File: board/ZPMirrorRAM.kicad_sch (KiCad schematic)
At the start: 17 parts, among them IC1 74LS189, IC2 74LS189, IC3 74LS189, IC4 74LS189, U13 74F08, U24 74F20, U25 74F02, U26 74LS154, U27 74F138

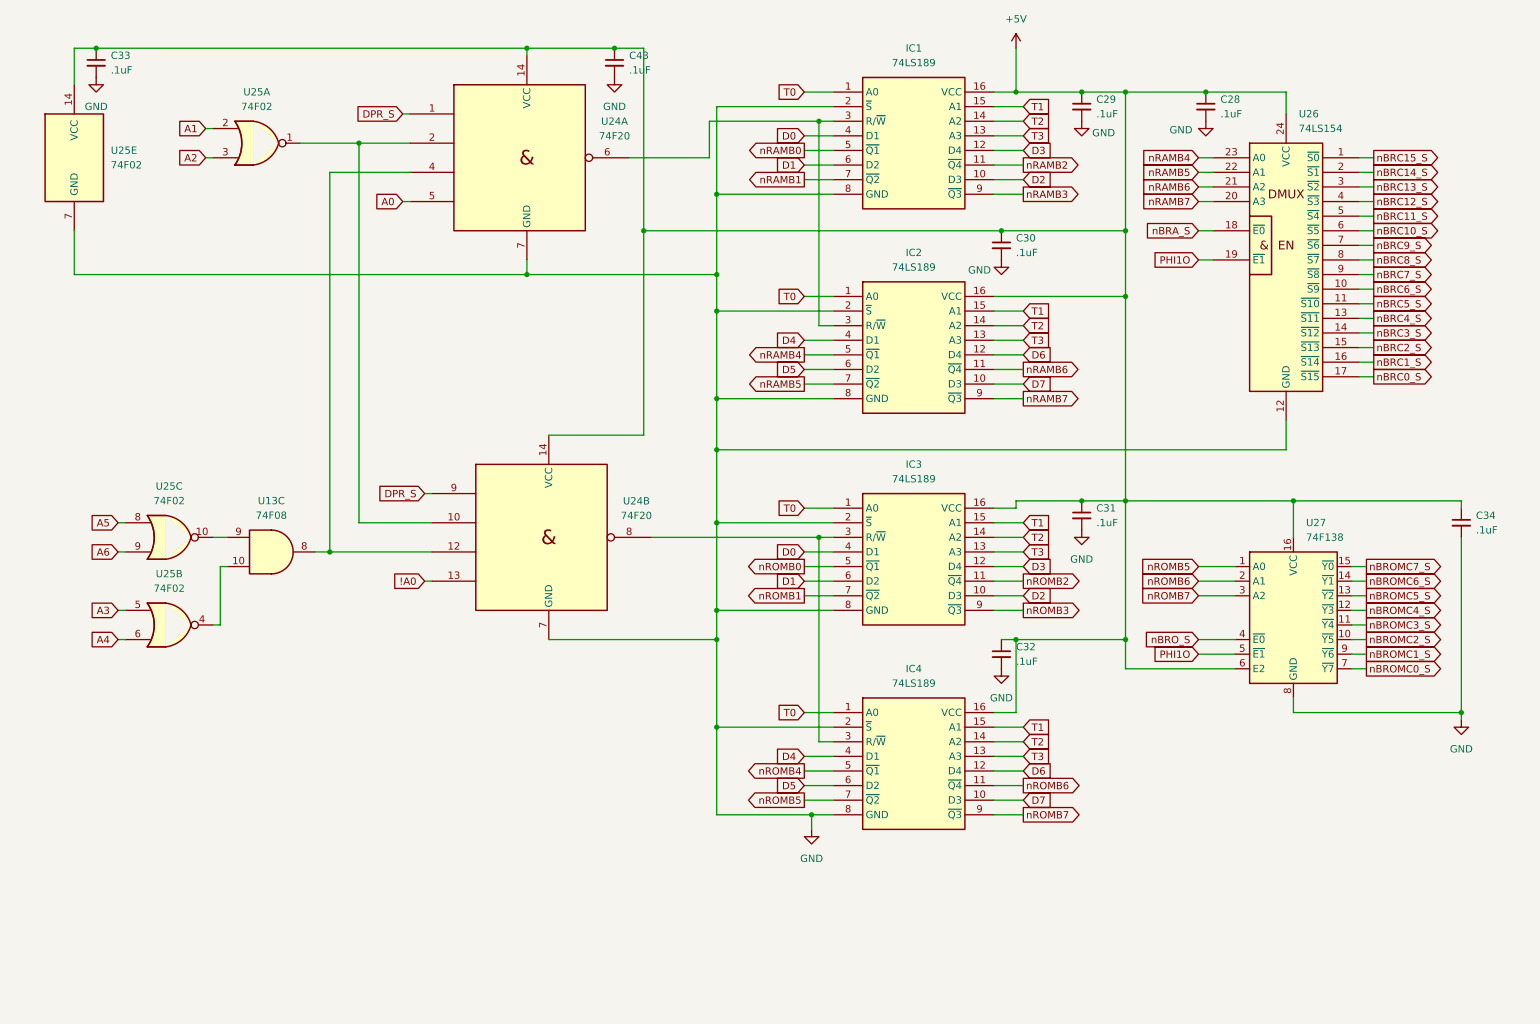
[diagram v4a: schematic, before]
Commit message: Schematic Bus updates, silkscreen updates, position tweaks, and other corrections.
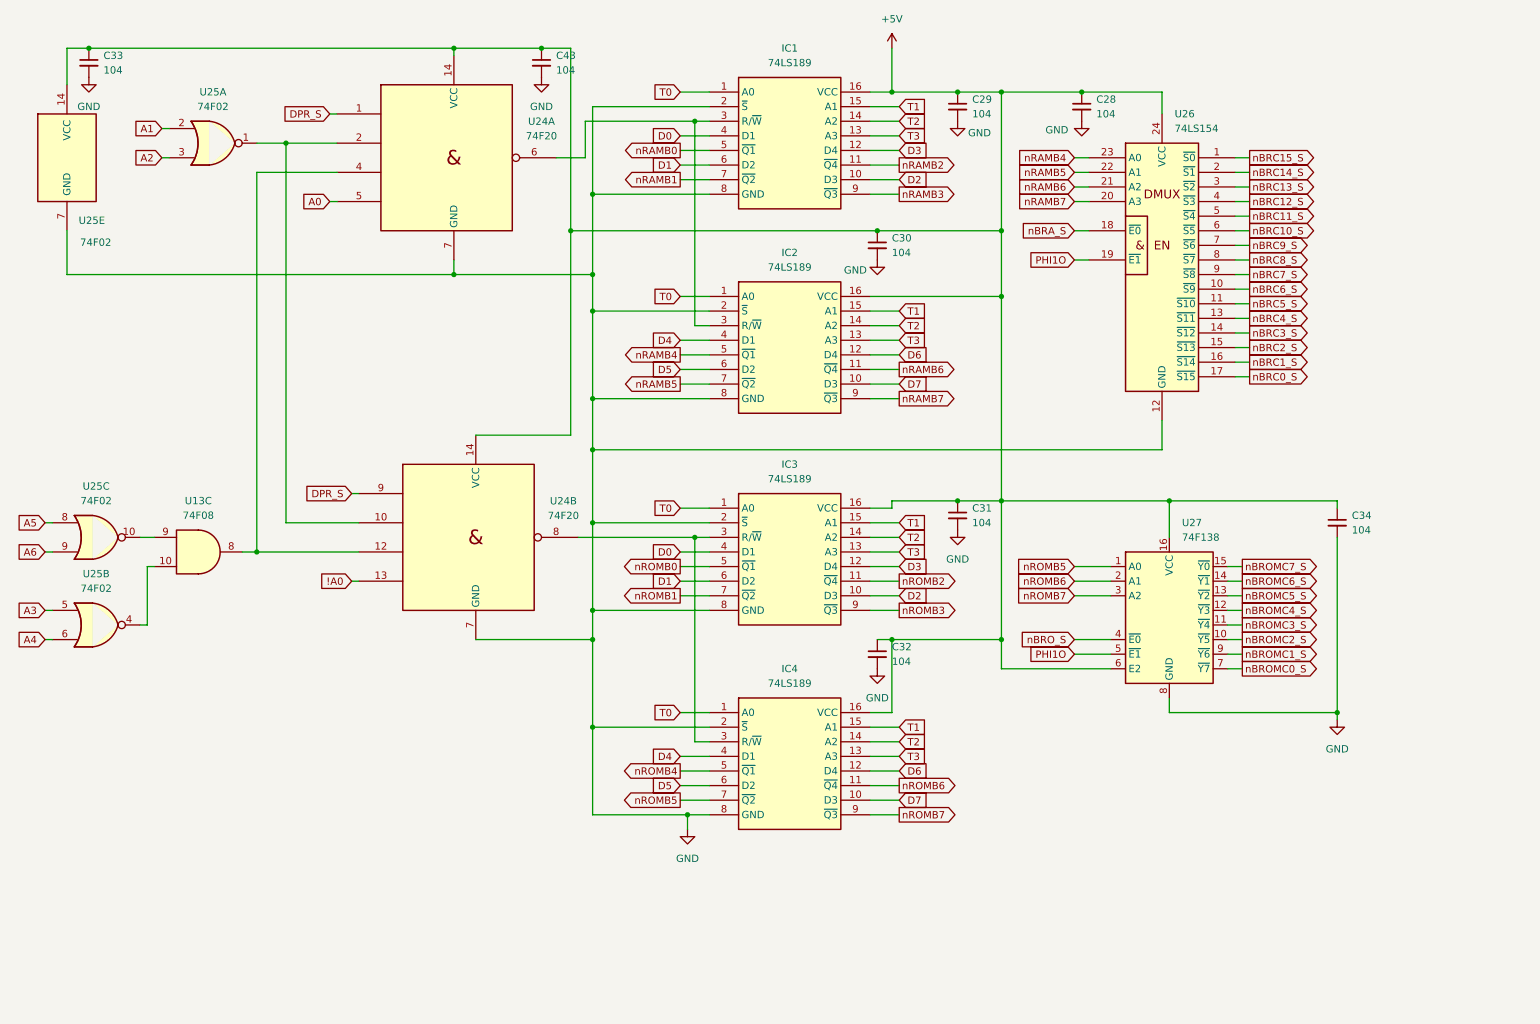
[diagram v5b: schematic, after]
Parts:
- C28, C29, C30, C31, C32, C33, C34, C43: value .1uF -> 104
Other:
- company: (none) -> Data Tuning
- title: (none) -> ZeroPage $00/$01 Mirror Memory and RAM/ROM Bank Logic
- moved on the sheet: C28, C29, C30, C31, C32, C33, C34, C43, IC1, IC2, IC3, IC4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

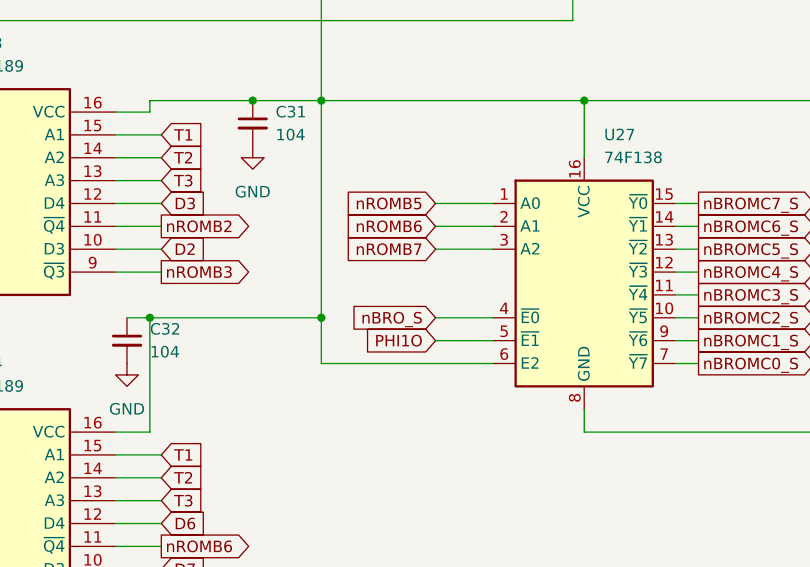
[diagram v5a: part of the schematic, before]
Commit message: Fixing nBROMD routing, removing unnecessary 7404, and minor other cleanup.
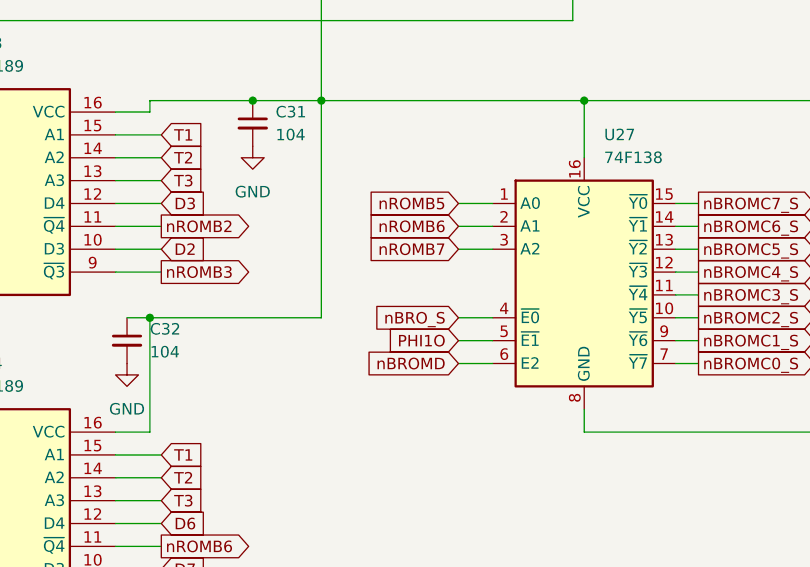
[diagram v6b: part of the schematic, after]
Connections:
- net +5V: no longer U27.6 (E2)
- new net nBROMD: U27.6 (E2)
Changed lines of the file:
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@@
-	)
-	(junction
-		(at 189.23 123.19)
-		(diameter 0)
-		(color 0 0 0 0)
 	)
 	(junction
@@
 	(wire
 		(pts
-			(xy 201.93 110.49) (xy 208.28 110.49)
+			(xy 204.47 110.49) (xy 208.28 110.49)
 		)
 		(stroke
@@
 	(wire
 		(pts
-			(xy 189.23 128.27) (xy 189.23 123.19)
-		)
-		(stroke
-			(width 0)
-			(type default)
-		)
-	)
-	(wire
-		(pts
 			(xy 133.35 40.64) (xy 138.43 40.64)
 		)
@@
 	(wire
 		(pts
-			(xy 201.93 113.03) (xy 208.28 113.03)
+			(xy 204.47 113.03) (xy 208.28 113.03)
 		)
 		(stroke
@@
 	(wire
 		(pts
-			(xy 208.28 128.27) (xy 189.23 128.27)
-		)
-		(stroke
-			(width 0)
-			(type default)
-		)
-	)
-	(wire
-		(pts
 			(xy 166.37 113.03) (xy 171.45 113.03)
 		)
@@
 	(wire
 		(pts
-			(xy 208.28 123.19) (xy 201.93 123.19)
+			(xy 208.28 123.19) (xy 204.47 123.19)
 		)
 		(stroke
@@
 	(wire
 		(pts
+			(xy 204.47 128.27) (xy 208.28 128.27)
+		)
+		(stroke
+			(width 0)
+			(type default)
+		)
+	)
+	(wire
+		(pts
 			(xy 232.41 49.53) (xy 229.87 49.53)
 		)
@@
 	(wire
 		(pts
-			(xy 201.93 125.73) (xy 208.28 125.73)
+			(xy 204.47 125.73) (xy 208.28 125.73)
 		)
 		(stroke
@@
 	(wire
 		(pts
-			(xy 201.93 115.57) (xy 208.28 115.57)
+			(xy 204.47 115.57) (xy 208.28 115.57)
 		)
 		(stroke
@@
 	(global_label "nROMB6"
 		(shape input)
-		(at 201.93 113.03 180)
+		(at 204.47 113.03 180)
 		(fields_autoplaced yes)
 		(effects
@@
 		)
 		(property "Intersheetrefs" "${INTERSHEET_REFS}"
-			(at 212.3537 113.03 0)
+			(at 214.8937 113.03 0)
 			(effects
 				(font
@@
 	(global_label "PHI1O"
 		(shape input)
-		(at 201.93 125.73 180)
+		(at 204.47 125.73 180)
 		(fields_autoplaced yes)
 		(effects
@@
 		)
 		(property "Intersheetrefs" "${INTERSHEET_REFS}"
-			(at 193.1995 125.73 0)
+			(at 195.7395 125.73 0)
 			(effects
 				(font
@@
 	(global_label "nROMB7"
 		(shape input)
-		(at 201.93 115.57 180)
+		(at 204.47 115.57 180)
 		(fields_autoplaced yes)
 		(effects
@@
 		)
 		(property "Intersheetrefs" "${INTERSHEET_REFS}"
-			(at 212.3537 115.57 0)
+			(at 214.8937 115.57 0)
 			(effects
 				(font
@@
 	(global_label "nROMB5"
 		(shape input)
-		(at 201.93 110.49 180)
+		(at 204.47 110.49 180)
 		(fields_autoplaced yes)
 		(effects
@@
 		)
 		(property "Intersheetrefs" "${INTERSHEET_REFS}"
-			(at 191.5063 110.49 0)
+			(at 194.0463 110.49 0)
 			(effects
 				(font
@@
 		)
 	)
+	(global_label "nBROMD"
+		(shape input)
+		(at 204.47 128.27 180)
+		(fields_autoplaced yes)
+		(effects
+			(font
+				(size 1.27 1.27)
+			)
+			(justify right)
+		)
+		(property "Intersheetrefs" "${INTERSHEET_REFS}"
+			(at 193.7439 128.27 0)
+			(effects
+				(font
+					(size 1.27 1.27)
+				)
+				(justify right)
+				(hide yes)
+			)
+		)
+	)
 	(global_label "D2"
 		(shape input)
@@
 	(global_label "nBRO_S"
 		(shape input)
-		(at 201.93 123.19 180)
+		(at 204.47 123.19 180)
 		(fields_autoplaced yes)
 		(effects
@@
 		)
 		(property "Intersheetrefs" "${INTERSHEET_REFS}"
-			(at 191.7482 123.19 0)
-			(effects
-				(font
+			(at 194.2882 123.19 0)
+			(effects
+				(font

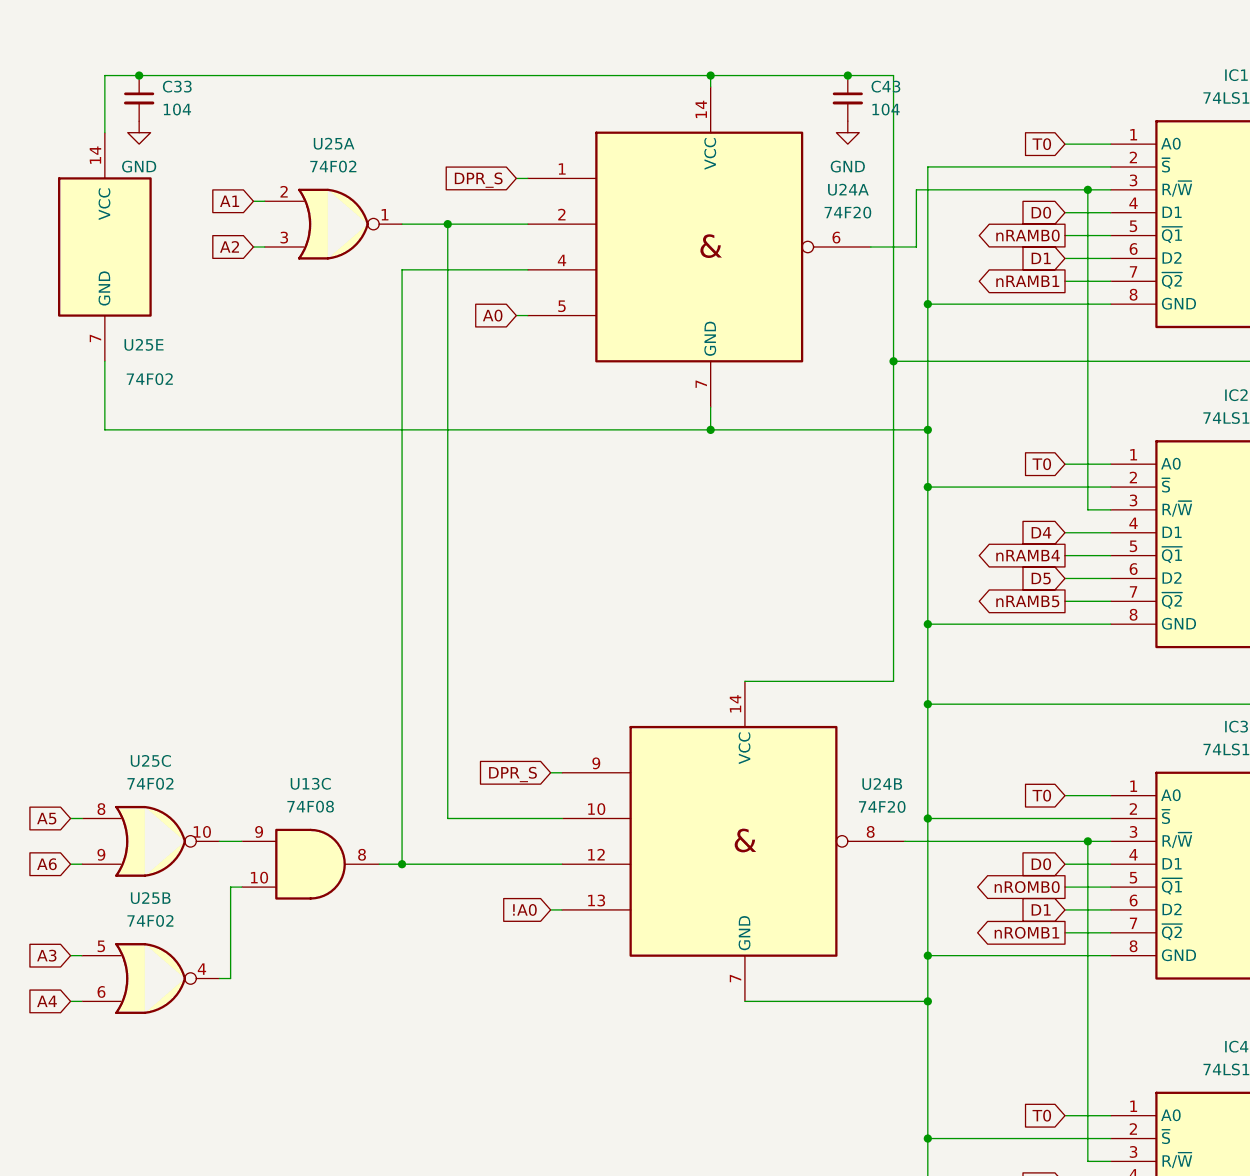
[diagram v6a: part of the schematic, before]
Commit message: Added VIA port A header and voltage protection diode package socket. Updated logic.
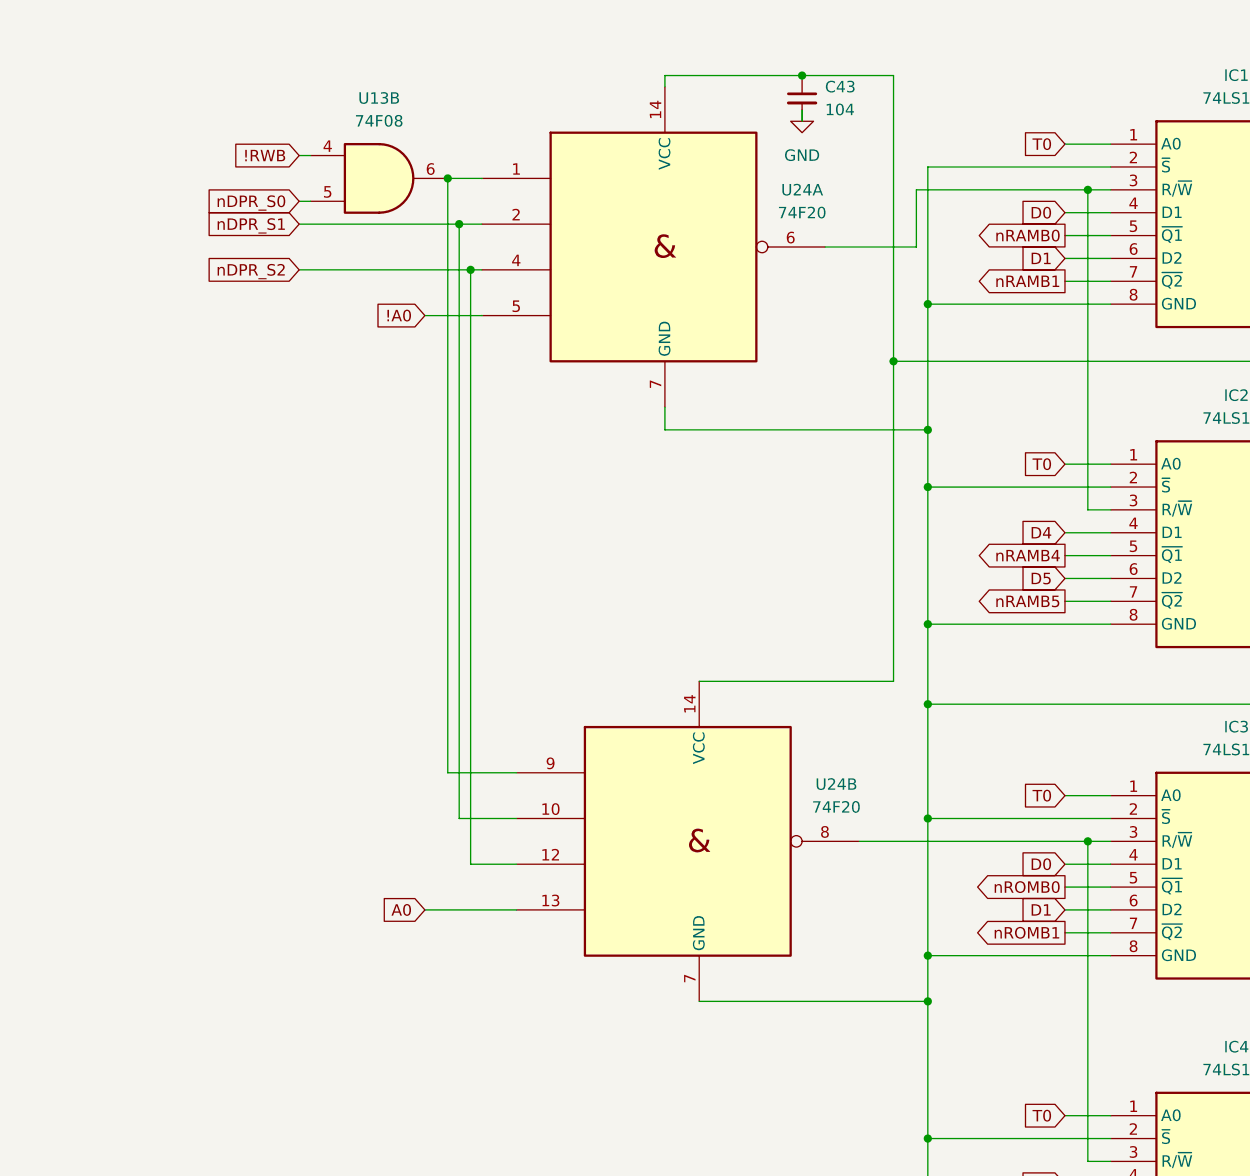
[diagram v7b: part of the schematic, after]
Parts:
- removed C33: 104, Capacitor_THT:C_Disc_D5.0mm_W2.5mm_P5.00mm, symbol Device:C_Small
- removed U13: 74F08, Package_DIP:DIP-14_W7.62mm_Socket_LongPads, symbol 74xx:74LS08
- removed U25: 74F02, Package_DIP:DIP-14_W7.62mm_Socket_LongPads, symbol 74xx:7402
- added U13: 74F08, Package_DIP:DIP-14_W7.62mm_Socket_LongPads, symbol 74xx:74LS08
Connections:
- net !A0: now also U24.5; no longer U24.13
- net A0: now also U24.13; no longer U24.5
- net nDPR_S1: now reaches U24.10, U24.2
- net nDPR_S2: now reaches U24.12, U24.4
- net DPR_S: no longer names the net of U24.1, U24.9
- net DPR_S: now also U13.6
- new net !RWB: U13.4
- new net nDPR_S0: U13.5
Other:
- moved on the sheet: C43, U24A, U24B
